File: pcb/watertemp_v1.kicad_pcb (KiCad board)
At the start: 2 copper layers, 56 x 90 mm, 50 parts, among them J1 RN2483 Ext, J2 SWD, J3 I2C, J4 UART1, J5 UART2, U1 LPC11U24FBD48, U2 RN2483, U3 SHT21, U4 LP5907-Q1, U5 DS18B20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

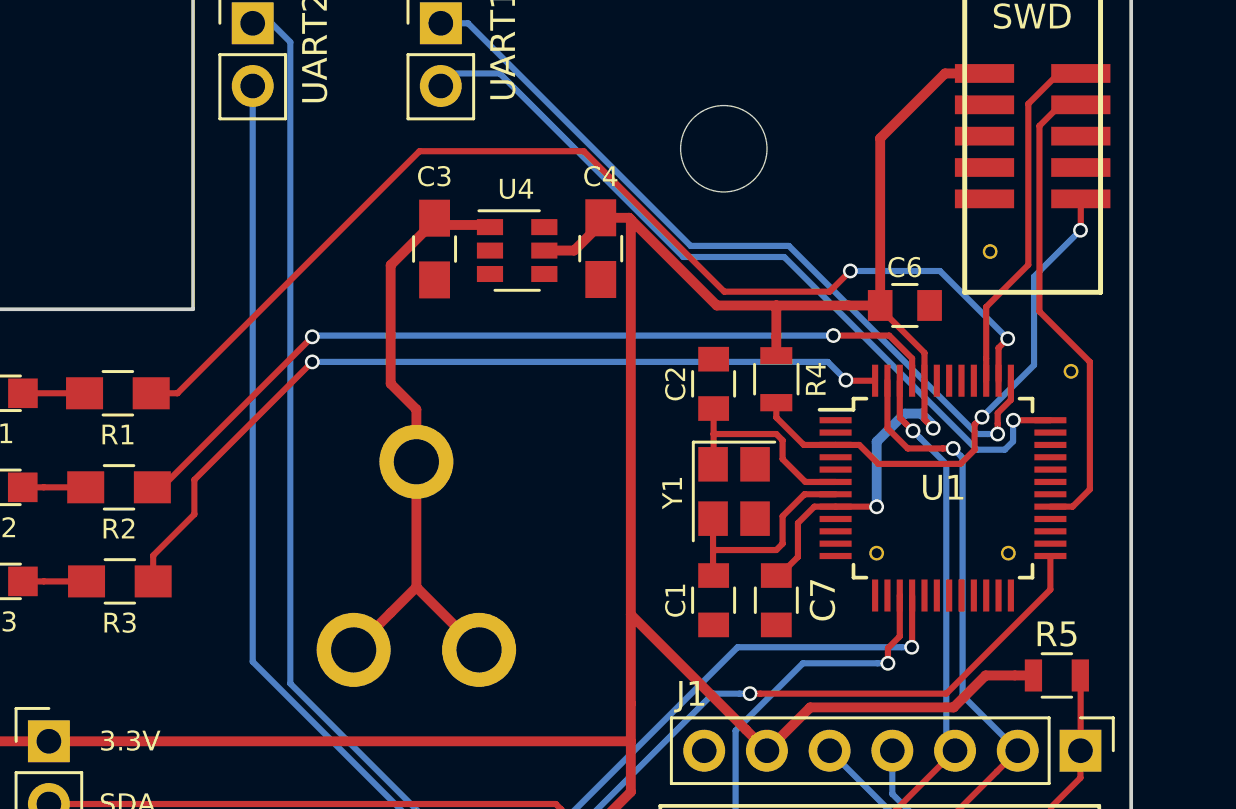
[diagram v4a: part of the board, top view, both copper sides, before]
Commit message: Add reverse polarity protection (fixes #11)
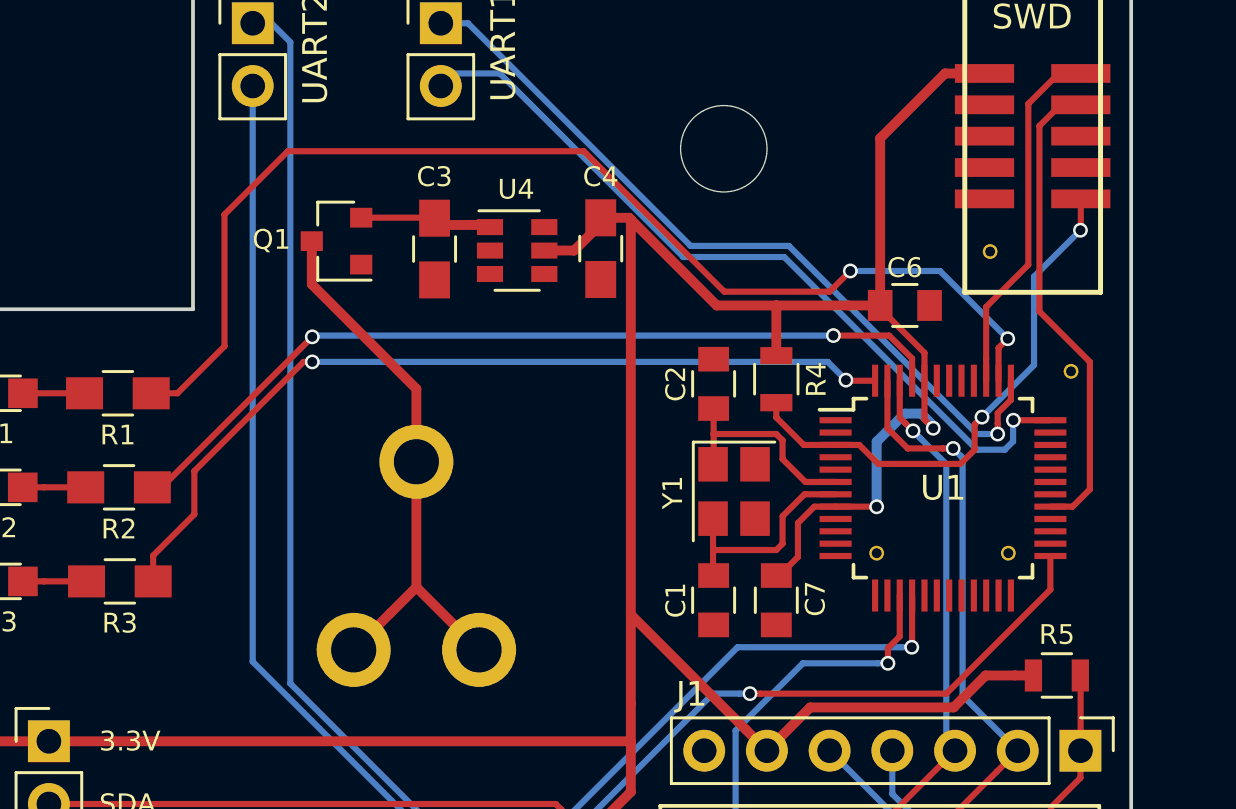
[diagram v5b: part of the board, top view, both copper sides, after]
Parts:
- added Q1: Q_PMOS_GSD, TO_SOT_Packages_SMD:SOT-23, F.Cu at (45.8, 51.2)
- AE1: value SMA -> Antenna_Shield
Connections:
- C3 pad 1: Net-(BT1-Pad1) -> Net-(C3-Pad1)
- U4 pad 1: Net-(BT1-Pad1) -> Net-(C3-Pad1)
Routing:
- net Net-(C3-Pad1): track 0.00 -> 5.35 mm
- net LED1: track 44.4 -> 47.6 mm
- net Net-(BT1-Pad1): track 25.4 -> 23.0 mm
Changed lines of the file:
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@@
 (kicad_pcb (version 4) (host pcbnew 4.0.6)
   (general
-    (links 0)
-    (no_connects 0)
+    (links 113)
+    (no_connects 3)
     (area 26.924999 39.924999 83.075001 130.075001)
     (thickness 1.6)
     (drawings 28)
-    (tracks 320)
+    (tracks 324)
     (zones 0)
-    (modules 50)
-    (nets 80)
+    (modules 51)
+    (nets 81)
   )
   (page A4)
@@
   (net 78 "Net-(D2-Pad2)")
   (net 79 "Net-(D3-Pad2)")
+  (net 80 "Net-(C3-Pad1)")
   (net_class Default "This is the default net class."
     (clearance 0.2)
@@
     (add_net "Net-(C1-Pad1)")
     (add_net "Net-(C2-Pad1)")
+    (add_net "Net-(C3-Pad1)")
     (add_net "Net-(D1-Pad2)")
     (add_net "Net-(D2-Pad2)")
@@
     (fp_line (start 2.25 0.87) (end -2.25 0.87) (layer F.CrtYd) (width 0.05))
     (pad 1 smd rect (at -1.25 0 270) (size 1.5 1.25) (layers F.Cu F.Paste F.Mask)
-      (net 3 "Net-(BT1-Pad1)"))
+      (net 80 "Net-(C3-Pad1)"))
     (pad 2 smd rect (at 1.25 0 270) (size 1.5 1.25) (layers F.Cu F.Paste F.Mask)
       (net 1 GND))
@@
     (fp_line (start 0.9 -1.55) (end 0.9 1.55) (layer F.Fab) (width 0.1))
     (pad 1 smd rect (at -1.1 -0.95) (size 1.06 0.65) (layers F.Cu F.Paste F.Mask)
-      (net 3 "Net-(BT1-Pad1)"))
+      (net 80 "Net-(C3-Pad1)"))
     (pad 2 smd rect (at -1.1 0) (size 1.06 0.65) (layers F.Cu F.Paste F.Mask)
       (net 1 GND))
@@
     (tags "capacitor 0805")
     (attr smd)
-    (fp_text reference C7 (at 0.016 1.905 90) (layer F.SilkS)
-      (effects (font (size 1 1) (thickness 0.15)))
+    (fp_text reference C7 (at 0.0635 1.5875 90) (layer F.SilkS)
+      (effects (font (size 0.8 0.8) (thickness 0.15)))
     )
     (fp_text value 100nF (at 0 1.75 90) (layer F.Fab)
@@
     (attr smd)
     (fp_text reference R5 (at 0 -1.65) (layer F.SilkS)
-      (effects (font (size 1 1) (thickness 0.15)))
+      (effects (font (size 0.8 0.8) (thickness 0.15)))
     )
     (fp_text value 10KΩ (at 0 1.75) (layer F.Fab)
@@
       (effects (font (size 1 1) (thickness 0.15)))
     )
-    (fp_text value SMA (at 3.53834 6.38032 270) (layer F.Fab)
+    (fp_text value Antenna_Shield (at 3.53834 6.38032 270) (layer F.Fab)
       (effects (font (size 1 1) (thickness 0.15)))
     )
@@
       (xy -9.75169 3.984735)) (layer B.SilkS) (width 0.01))
   )
+  (module TO_SOT_Packages_SMD:SOT-23 (layer F.Cu)
+    (at 45.8122 51.242 180)
+    (descr "SOT-23, Standard")
+    (tags SOT-23)
+    (attr smd)
+    (fp_text reference Q1 (at 2.6322 0.061 180) (layer F.SilkS)
+      (effects (font (size 0.8 0.8) (thickness 0.15)))
+    )
+    (fp_text value Q_PMOS_GSD (at 0 2.5 180) (layer F.Fab)
+      (effects (font (size 1 1) (thickness 0.15)))
+    )
+    (fp_text user %R (at 0 0 270) (layer F.Fab)
+      (effects (font (size 0.5 0.5) (thickness 0.075)))
+    )
+    (fp_line (start -0.7 -0.95) (end -0.7 1.5) (layer F.Fab) (width 0.1))
+    (fp_line (start -0.15 -1.52) (end 0.7 -1.52) (layer F.Fab) (width 0.1))
+    (fp_line (start -0.7 -0.95) (end -0.15 -1.52) (layer F.Fab) (width 0.1))
+    (fp_line (start 0.7 -1.52) (end 0.7 1.52) (layer F.Fab) (width 0.1))
+    (fp_line (start -0.7 1.52) (end 0.7 1.52) (layer F.Fab) (width 0.1))
+    (fp_line (start 0.76 1.58) (end 0.76 0.65) (layer F.SilkS) (width 0.12))
+    (fp_line (start 0.76 -1.58) (end 0.76 -0.65) (layer F.SilkS) (width 0.12))
+    (fp_line (start -1.7 -1.75) (end 1.7 -1.75) (layer F.CrtYd) (width 0.05))
+    (fp_line (start 1.7 -1.75) (end 1.7 1.75) (layer F.CrtYd) (width 0.05))
+    (fp_line (start 1.7 1.75) (end -1.7 1.75) (layer F.CrtYd) (width 0.05))
+    (fp_line (start -1.7 1.75) (end -1.7 -1.75) (layer F.CrtYd) (width 0.05))
+    (fp_line (start 0.76 -1.58) (end -1.4 -1.58) (layer F.SilkS) (width 0.12))
+    (fp_line (start 0.76 1.58) (end -0.7 1.58) (layer F.SilkS) (width 0.12))
+    (pad 1 smd rect (at -1 -0.95 180) (size 0.9 0.8) (layers F.Cu F.Paste F.Mask)
+      (net 1 GND))
+    (pad 2 smd rect (at -1 0.95 180) (size 0.9 0.8) (layers F.Cu F.Paste F.Mask)
+      (net 80 "Net-(C3-Pad1)"))
+    (pad 3 smd rect (at 1 0 180) (size 0.9 0.8) (layers F.Cu F.Paste F.Mask)
+      (net 3 "Net-(BT1-Pad1)"))
+    (model ${KISYS3DMOD}/TO_SOT_Packages_SMD.3dshapes/SOT-23.wrl
+      (at (xyz 0 0 0))
+      (scale (xyz 1 1 1))
+      (rotate (xyz 0 0 0))
+    )
+  )
   (gr_text https://github.com/coredump-ch/watertemp-hardware (at 30.226 77.851 90) (layer B.SilkS)
     (effects (font (size 1 1) (thickness 0.15)) (justify mirror))
@@
   (segment (start 64.8462 104.5718) (end 66.548 102.87) (width 1.016) (layer F.Cu) (net 2))
   (segment (start 66.548 102.87) (end 66.548 100.7872) (width 1.016) (layer F.Cu) (net 2))
-  (segment (start 49.0474 60.1786) (end 49.0474 58.05728) (width 0.4) (layer F.Cu) (net 3))
-  (segment (start 49.0474 58.05728) (end 48.006 57.01588) (width 0.4) (layer F.Cu) (net 3))
-  (segment (start 48.006 57.01588) (end 48.006 52.215) (width 0.4) (layer F.Cu) (net 3))
-  (segment (start 48.006 52.215) (end 49.659 50.562) (width 0.4) (layer F.Cu) (net 3))
-  (segment (start 49.659 50.562) (end 49.784 50.562) (width 0.4) (layer F.Cu) (net 3))
+  (segment (start 49.0474 60.1786) (end 49.0474 57.2262) (width 0.4) (layer F.Cu) (net 3))
+  (segment (start 49.0474 57.2262) (end 44.8122 52.991) (width 0.4) (layer F.Cu) (net 3))
+  (segment (start 44.8122 52.991) (end 44.8122 51.242) (width 0.4) (layer F.Cu) (net 3))
   (segment (start 46.5074 67.7986) (end 48.007399 66.298601) (width 0.4) (layer F.Cu) (net 3))
   (segment (start 48.007399 66.298601) (end 49.0474 65.2586) (width 0.4) (layer F.Cu) (net 3))
   (segment (start 49.0474 60.1786) (end 49.0474 65.2586) (width 0.4) (layer F.Cu) (net 3))
   (segment (start 49.0474 65.2586) (end 51.5874 67.7986) (width 0.4) (layer F.Cu) (net 3))
-  (segment (start 49.8348 50.5874) (end 51.959 50.5874) (width 0.4) (layer F.Cu) (net 3))
-  (segment (start 51.959 50.5874) (end 52.0446 50.673) (width 0.4) (layer F.Cu) (net 3))
   (segment (start 61.065 63.754) (end 63.627 63.754) (width 0.25) (layer F.Cu) (net 4))
   (segment (start 63.627 63.754) (end 63.881 63.5) (width 0.25) (layer F.Cu) (net 4))
@@
   (segment (start 73.2284 58.496) (end 73.2282 58.4962) (width 0.25) (layer F.Cu) (net 21))
   (segment (start 74.728 58.496) (end 73.2284 58.496) (width 0.25) (layer F.Cu) (net 21))
-  (segment (start 38.307 57.404) (end 39.37 57.404) (width 0.25) (layer F.Cu) (net 22))
-  (segment (start 39.37 57.404) (end 49.1744 47.5996) (width 0.25) (layer F.Cu) (net 22))
-  (segment (start 49.1744 47.5996) (end 55.8292 47.5996) (width 0.25) (layer F.Cu) (net 22))
-  (segment (start 55.8292 47.5996) (end 61.5188 53.2892) (width 0.25) (layer F.Cu) (net 22))
-  (segment (start 61.5188 53.2892) (end 65.786 53.2892) (width 0.25) (layer F.Cu) (net 22))
-  (segment (start 65.786 53.2892) (end 66.6242 52.451) (width 0.25) (layer F.Cu) (net 22))
+  (segment (start 66.6242 52.451) (end 65.786 53.2892) (width 0.25) (layer F.Cu) (net 22))
+  (segment (start 65.786 53.2892) (end 61.5188 53.2892) (width 0.25) (layer F.Cu) (net 22))
+  (segment (start 41.275 50.165) (end 41.275 55.499) (width 0.25) (layer F.Cu) (net 22))
+  (segment (start 39.37 57.404) (end 38.307 57.404) (width 0.25) (layer F.Cu) (net 22))
+  (segment (start 61.5188 53.2892) (end 55.8292 47.5996) (width 0.25) (layer F.Cu) (net 22))
+  (segment (start 55.8292 47.5996) (end 43.8404 47.5996) (width 0.25) (layer F.Cu) (net 22))
+  (segment (start 43.8404 47.5996) (end 41.275 50.165) (width 0.25) (layer F.Cu) (net 22))
+  (segment (start 41.275 55.499) (end 39.37 57.404) (width 0.25) (layer F.Cu) (net 22))
   (segment (start 72.9996 55.1942) (end 70.2564 52.451) (width 0.25) (layer B.Cu) (net 22))
   (segment (start 70.2564 52.451) (end 66.6242 52.451) (width 0.25) (layer B.Cu) (net 22))
@@
   (segment (start 68.1992 55.0672) (end 65.9384 55.0672) (width 0.25) (layer F.Cu) (net 23))
   (via (at 65.9384 55.0672) (size 0.6) (drill 0.4) (layers F.Cu B.Cu) (net 23))
-  (segment (start 38.387 63.975) (end 38.387 65.024) (width 0.25) (layer F.Cu) (net 24))
+  (via (at 44.831 56.134) (size 0.6) (drill 0.4) (layers F.Cu B.Cu) (net 24))
+  (segment (start 65.7098 56.134) (end 44.831 56.134) (width 0.25) (layer B.Cu) (net 24))
+  (segment (start 44.831 56.134) (end 44.4754 56.134) (width 0.25) (layer F.Cu) (net 24))
+  (segment (start 44.4754 56.134) (end 40.0558 60.5536) (width 0.25) (layer F.Cu) (net 24))
+  (segment (start 40.0558 60.5536) (end 40.0558 62.3062) (width 0.25) (layer F.Cu) (net 24))
   (segment (start 40.0558 62.3062) (end 38.387 63.975) (width 0.25) (layer F.Cu) (net 24))
-  (segment (start 40.0558 60.9092) (end 40.0558 62.3062) (width 0.25) (layer F.Cu) (net 24))
-  (segment (start 44.831 56.134) (end 40.0558 60.9092) (width 0.25) (layer F.Cu) (net 24))
+  (segment (start 38.387 63.975) (end 38.387 65.024) (width 0.25) (layer F.Cu) (net 24))
   (segment (start 66.4464 56.8706) (end 65.7098 56.134) (width 0.25) (layer B.Cu) (net 24))
-  (segment (start 65.7098 56.134) (end 44.831 56.134) (width 0.25) (layer B.Cu) (net 24))
-  (via (at 44.831 56.134) (size 0.6) (drill 0.4) (layers F.Cu B.Cu) (net 24))
   (segment (start 67.628 56.896) (end 66.4718 56.896) (width 0.25) (layer F.Cu) (net 24))
   (segment (start 66.4718 56.896) (end 66.4464 56.8706) (width 0.25) (layer F.Cu) (net 24))
@@
   (segment (start 33.1118 65.024) (end 33.9618 65.024) (width 0.25) (layer F.Cu) (net 79))
   (segment (start 33.9618 65.024) (end 35.687 65.024) (width 0.25) (layer F.Cu) (net 79))
+  (segment (start 46.8122 50.292) (end 49.764 50.292) (width 0.25) (layer F.Cu) (net 80))
+  (segment (start 49.764 50.292) (end 49.784 50.312) (width 0.25) (layer F.Cu) (net 80))
+  (segment (start 49.659 50.562) (end 49.784 50.562) (width 0.4) (layer F.Cu) (net 80))
+  (segment (start 49.8348 50.5874) (end 51.959 50.5874) (width 0.4) (layer F.Cu) (net 80))
+  (segment (start 51.959 50.5874) (end 52.0446 50.673) (width 0.4) (layer F.Cu) (net 80))
   (zone (net 1) (net_name GND) (layer B.Cu) (hatch edge 0.508)
     (connect_pads (clearance 0.508))

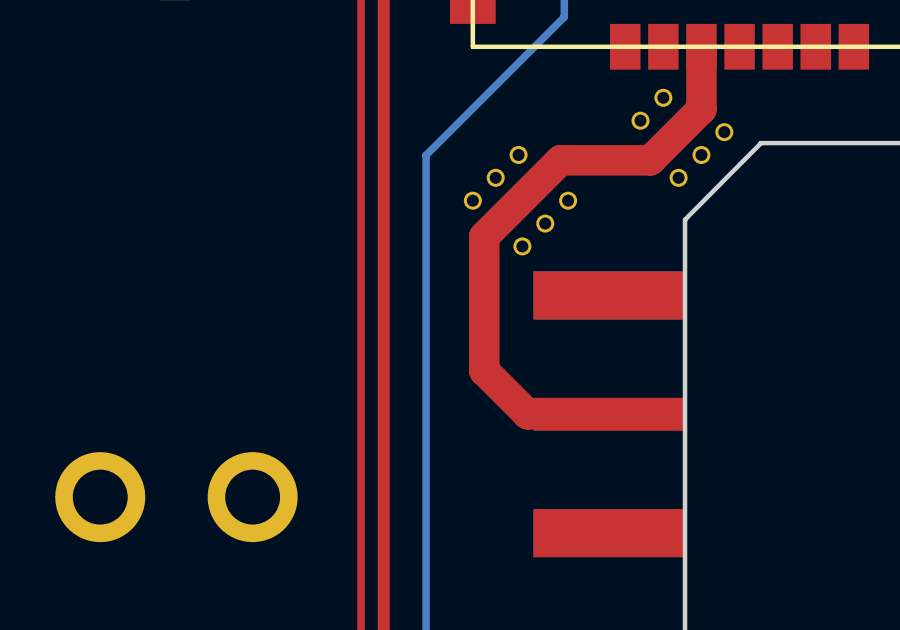
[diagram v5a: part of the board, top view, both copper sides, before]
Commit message: Add more stitching vias (fixes #6)
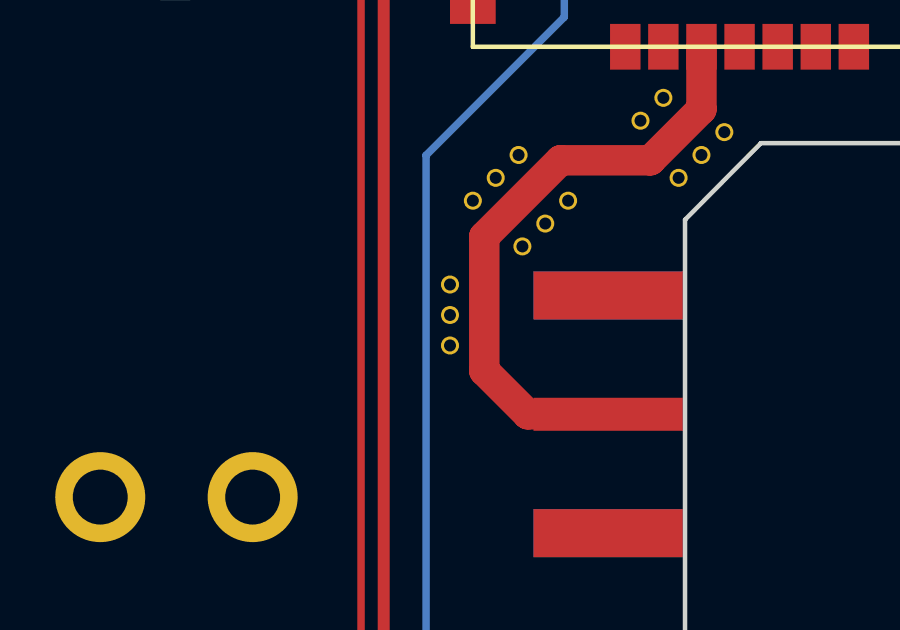
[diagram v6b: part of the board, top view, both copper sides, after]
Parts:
- added REF**: VIA-0.6mm, StitchingVia:VIA-0.6mm, F.Cu at (58.2, 110.7)
- added REF**: VIA-0.6mm, StitchingVia:VIA-0.6mm, F.Cu at (58.2, 109.7)
- added REF**: VIA-0.6mm, StitchingVia:VIA-0.6mm, F.Cu at (58.2, 108.7)
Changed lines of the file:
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@@
   (general
     (links 113)
-    (no_connects 3)
+    (no_connects 0)
     (area 26.924999 39.924999 83.075001 130.075001)
     (thickness 1.6)
@@
     (tracks 324)
     (zones 0)
-    (modules 51)
+    (modules 54)
     (nets 81)
   )
@@
     (add_net "Net-(AE1-Pad1)")
   )
+  (module StitchingVia:VIA-0.6mm (layer F.Cu)
+    (at 58.166 110.744)
+    (fp_text reference REF** (at 0 1.27) (layer F.SilkS) hide
+      (effects (font (size 1 1) (thickness 0.15)))
+    )
+    (fp_text value VIA-0.6mm (at 0 -1.27) (layer F.Fab) hide
+      (effects (font (size 1 1) (thickness 0.15)))
+    )
+    (pad 1 thru_hole circle (at 0 0) (size 0.6 0.6) (drill 0.4) (layers *.Cu)
+      (net 1 GND) (zone_connect 2))
+  )
+  (module StitchingVia:VIA-0.6mm (layer F.Cu)
+    (at 58.166 109.728)
+    (fp_text reference REF** (at 0 1.27) (layer F.SilkS) hide
+      (effects (font (size 1 1) (thickness 0.15)))
+    )
+    (fp_text value VIA-0.6mm (at 0 -1.27) (layer F.Fab) hide
+      (effects (font (size 1 1) (thickness 0.15)))
+    )
+    (pad 1 thru_hole circle (at 0 0) (size 0.6 0.6) (drill 0.4) (layers *.Cu)
+      (net 1 GND) (zone_connect 2))
+  )
+  (module StitchingVia:VIA-0.6mm (layer F.Cu)
+    (at 58.166 108.712)
+    (fp_text reference REF** (at 0 1.27) (layer F.SilkS) hide
+      (effects (font (size 1 1) (thickness 0.15)))
+    )
+    (fp_text value VIA-0.6mm (at 0 -1.27) (layer F.Fab) hide
+      (effects (font (size 1 1) (thickness 0.15)))
+    )
+    (pad 1 thru_hole circle (at 0 0) (size 0.6 0.6) (drill 0.4) (layers *.Cu)
+      (net 1 GND) (zone_connect 2))
+  )
   (module Capacitors_SMD:C_0805_HandSoldering (layer F.Cu)
